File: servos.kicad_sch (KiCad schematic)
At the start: 40 parts, among them J10 Conn_01x03, J11 Conn_01x03, J6 Conn_01x03, J7 Conn_01x03, J8 Conn_01x03, J9 Conn_01x03, U10 INA745A, U11 INA745A, U12 INA745A, U13 INA745A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

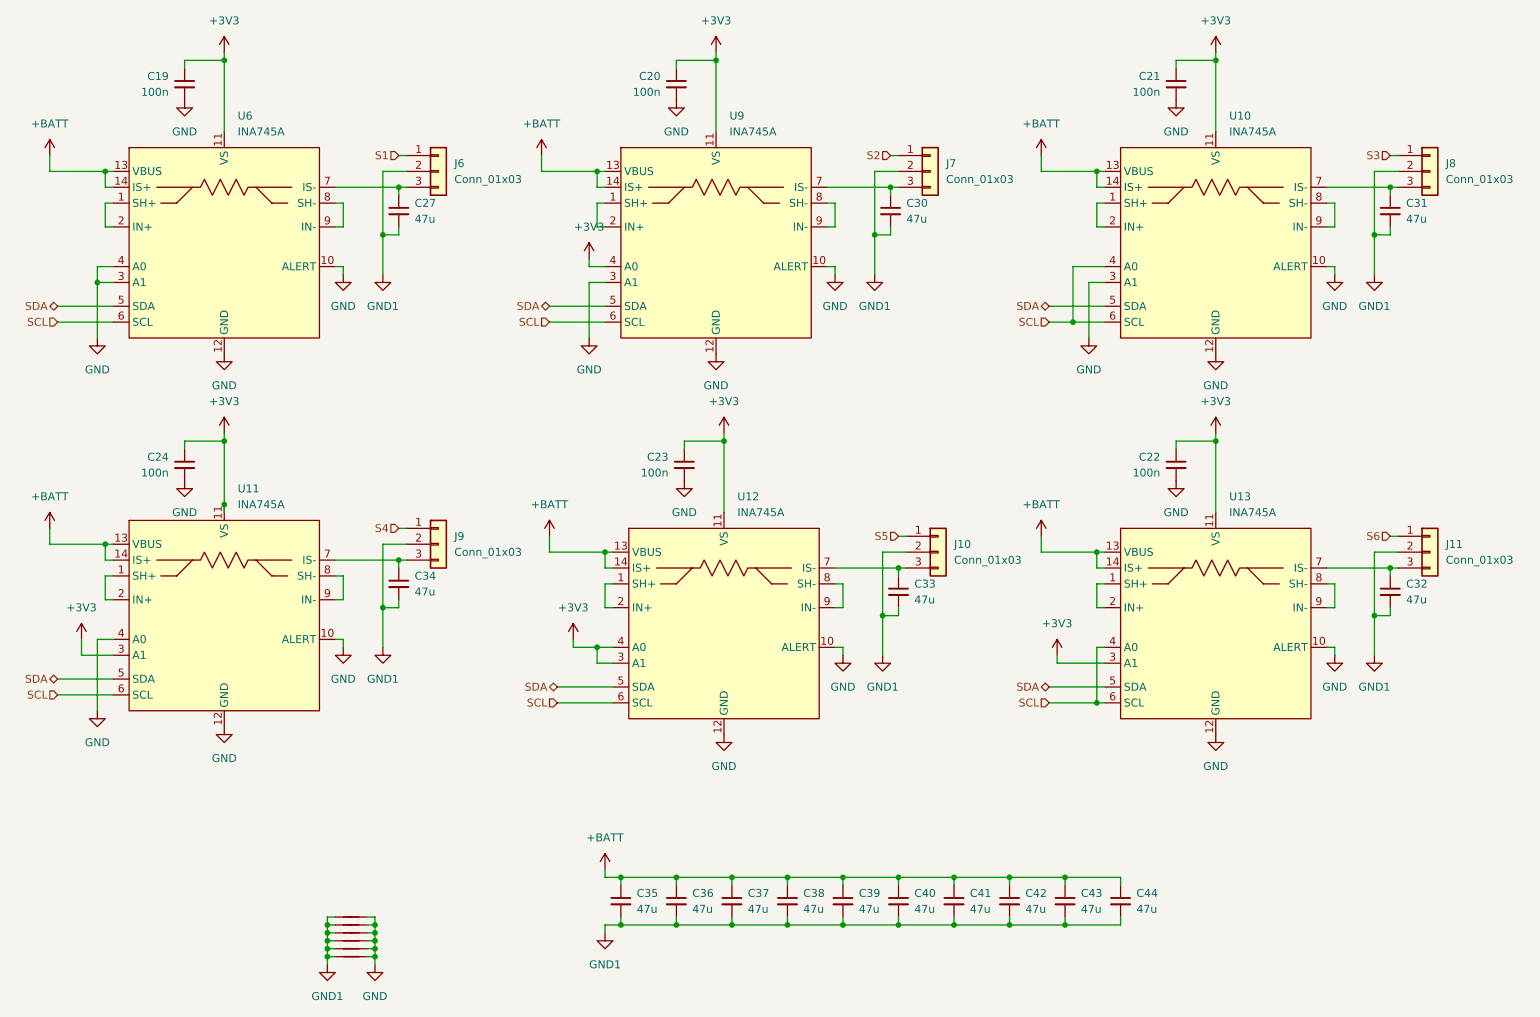
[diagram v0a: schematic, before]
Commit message: switched to global labels for SPI and I2C, added labels for servos
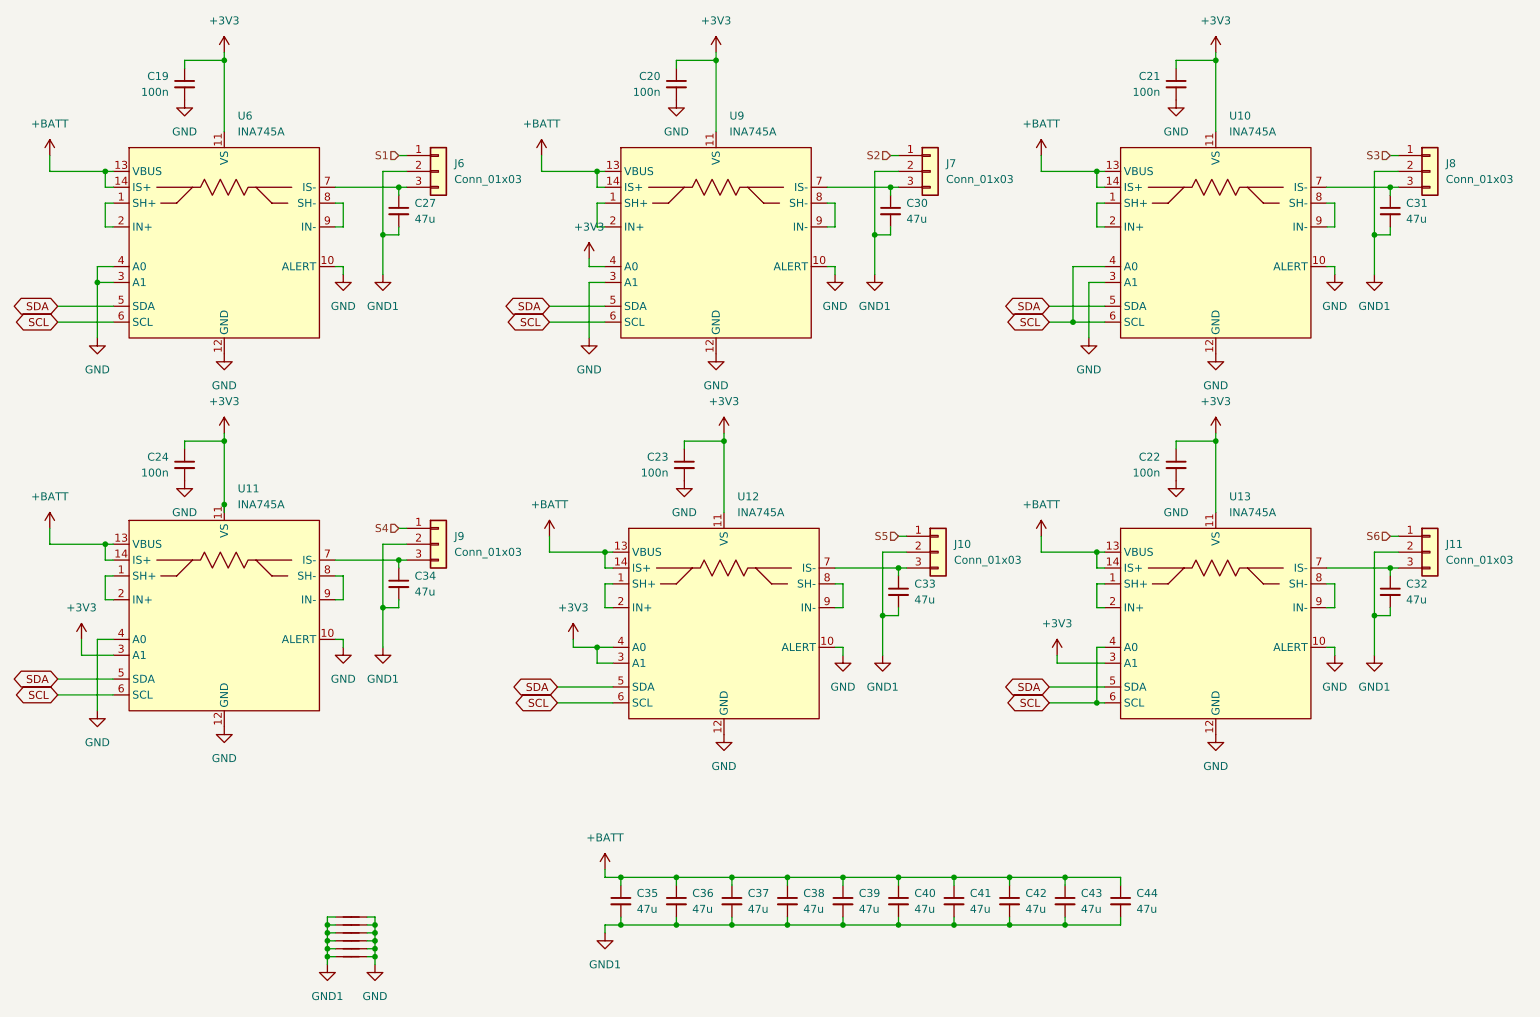
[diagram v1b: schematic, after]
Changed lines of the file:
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@@
 		)
 	)
-	(hierarchical_label "SCL"
-		(shape input)
+	(global_label "SDA"
+		(shape bidirectional)
+		(at 113.03 139.7 180)
+		(fields_autoplaced yes)
+		(effects
+			(font
+				(size 1.27 1.27)
+			)
+			(justify right)
+		)
+		(property "Intersheetrefs" "${INTERSHEET_REFS}"
+			(at 105.3654 139.7 0)
+			(effects
+				(font
+					(size 1.27 1.27)
+				)
+				(justify right)
+				(hide yes)
+			)
+		)
+	)
+	(global_label "SCL"
+		(shape bidirectional)
+		(at 113.03 142.24 180)
+		(fields_autoplaced yes)
+		(effects
+			(font
+				(size 1.27 1.27)
+			)
+			(justify right)
+		)
+		(property "Intersheetrefs" "${INTERSHEET_REFS}"
+			(at 105.4259 142.24 0)
+			(effects
+				(font
+					(size 1.27 1.27)
+				)
+				(justify right)
+				(hide yes)
+			)
+		)
+	)
+	(global_label "SCL"
+		(shape bidirectional)
+		(at 33.02 81.28 180)
+		(fields_autoplaced yes)
+		(effects
+			(font
+				(size 1.27 1.27)
+			)
+			(justify right)
+		)
+		(property "Intersheetrefs" "${INTERSHEET_REFS}"
+			(at 25.4159 81.28 0)
+			(effects
+				(font
+					(size 1.27 1.27)
+				)
+				(justify right)
+				(hide yes)
+			)
+		)
+	)
+	(global_label "SDA"
+		(shape bidirectional)
+		(at 111.76 78.74 180)
+		(fields_autoplaced yes)
+		(effects
+			(font
+				(size 1.27 1.27)
+			)
+			(justify right)
+		)
+		(property "Intersheetrefs" "${INTERSHEET_REFS}"
+			(at 104.0954 78.74 0)
+			(effects
+				(font
+					(size 1.27 1.27)
+				)
+				(justify right)
+				(hide yes)
+			)
+		)
+	)
+	(global_label "SCL"
+		(shape bidirectional)
+		(at 33.02 140.97 180)
+		(fields_autoplaced yes)
+		(effects
+			(font
+				(size 1.27 1.27)
+			)
+			(justify right)
+		)
+		(property "Intersheetrefs" "${INTERSHEET_REFS}"
+			(at 25.4159 140.97 0)
+			(effects
+				(font
+					(size 1.27 1.27)
+				)
+				(justify right)
+				(hide yes)
+			)
+		)
+	)
+	(global_label "SDA"
+		(shape bidirectional)
+		(at 191.77 139.7 180)
+		(fields_autoplaced yes)
+		(effects
+			(font
+				(size 1.27 1.27)
+			)
+			(justify right)
+		)
+		(property "Intersheetrefs" "${INTERSHEET_REFS}"
+			(at 184.1054 139.7 0)
+			(effects
+				(font
+					(size 1.27 1.27)
+				)
+				(justify right)
+				(hide yes)
+			)
+		)
+	)
+	(global_label "SCL"
+		(shape bidirectional)
 		(at 191.77 81.28 180)
-		(effects
-			(font
-				(size 1.27 1.27)
-			)
-			(justify right)
-		)
-	)
-	(hierarchical_label "SDA"
+		(fields_autoplaced yes)
+		(effects
+			(font
+				(size 1.27 1.27)
+			)
+			(justify right)
+		)
+		(property "Intersheetrefs" "${INTERSHEET_REFS}"
+			(at 184.1659 81.28 0)
+			(effects
+				(font
+					(size 1.27 1.27)
+				)
+				(justify right)
+				(hide yes)
+			)
+		)
+	)
+	(global_label "SDA"
+		(shape bidirectional)
+		(at 191.77 78.74 180)
+		(fields_autoplaced yes)
+		(effects
+			(font
+				(size 1.27 1.27)
+			)
+			(justify right)
+		)
+		(property "Intersheetrefs" "${INTERSHEET_REFS}"
+			(at 184.1054 78.74 0)
+			(effects
+				(font
+					(size 1.27 1.27)
+				)
+				(justify right)
+				(hide yes)
+			)
+		)
+	)
+	(global_label "SCL"
+		(shape bidirectional)
+		(at 111.76 81.28 180)
+		(fields_autoplaced yes)
+		(effects
+			(font
+				(size 1.27 1.27)
+			)
+			(justify right)
+		)
+		(property "Intersheetrefs" "${INTERSHEET_REFS}"
+			(at 104.1559 81.28 0)
+			(effects
+				(font
+					(size 1.27 1.27)
+				)
+				(justify right)
+				(hide yes)
+			)
+		)
+	)
+	(global_label "SDA"
 		(shape bidirectional)
 		(at 33.02 138.43 180)
-		(effects
-			(font
-				(size 1.27 1.27)
-			)
-			(justify right)
-		)
-	)
-	(hierarchical_label "SDA"
+		(fields_autoplaced yes)
+		(effects
+			(font
+				(size 1.27 1.27)
+			)
+			(justify right)
+		)
+		(property "Intersheetrefs" "${INTERSHEET_REFS}"
+			(at 25.3554 138.43 0)
+			(effects
+				(font
+					(size 1.27 1.27)
+				)
+				(justify right)
+				(hide yes)
+			)
+		)
+	)
+	(global_label "SCL"
+		(shape bidirectional)
+		(at 191.77 142.24 180)
+		(fields_autoplaced yes)
+		(effects
+			(font
+				(size 1.27 1.27)
+			)
+			(justify right)
+		)
+		(property "Intersheetrefs" "${INTERSHEET_REFS}"
+			(at 184.1659 142.24 0)
+			(effects
+				(font
+					(size 1.27 1.27)
+				)
+				(justify right)
+				(hide yes)
+			)
+		)
+	)
+	(global_label "SDA"
 		(shape bidirectional)
 		(at 33.02 78.74 180)
-		(effects
-			(font
-				(size 1.27 1.27)
-			)
-			(justify right)
-		)
-	)
-	(hierarchical_label "SCL"
-		(shape input)
-		(at 191.77 142.24 180)
-		(effects
-			(font
-				(size 1.27 1.27)
-			)
-			(justify right)
-		)
-	)
-	(hierarchical_label "SCL"
-		(shape input)
-		(at 33.02 81.28 180)
-		(effects
-			(font
-				(size 1.27 1.27)
-			)
-			(justify right)
-		)
-	)
-	(hierarchical_label "SDA"
-		(shape bidirectional)
-		(at 111.76 78.74 180)
-		(effects
-			(font
-				(size 1.27 1.27)
-			)
-			(justify right)
+		(fields_autoplaced yes)
+		(effects
+			(font
+				(size 1.27 1.27)
+			)
+			(justify right)
+		)
+		(property "Intersheetrefs" "${INTERSHEET_REFS}"
+			(at 25.3554 78.74 0)
+			(effects
+				(font
+					(size 1.27 1.27)
+				)
+				(justify right)
+				(hide yes)
+			)
 		)
 	)
@@
 		)
 	)
-	(hierarchical_label "SCL"
-		(shape input)
-		(at 33.02 140.97 180)
-		(effects
-			(font
-				(size 1.27 1.27)
-			)
-			(justify right)
-		)
-	)
-	(hierarchical_label "SDA"
-		(shape bidirectional)
-		(at 113.03 139.7 180)
-		(effects
-			(font
-				(size 1.27 1.27)
-			)
-			(justify right)
-		)
-	)
 	(hierarchical_label "S3"
 		(shape input)
@@
 		)
 	)
-	(hierarchical_label "SDA"
-		(shape bidirectional)
-		(at 191.77 78.74 180)
-		(effects
-			(font
-				(size 1.27 1.27)
-			)
-			(justify right)
-		)
-	)
 	(hierarchical_label "S2"
 		(shape input)
@@
 		(effects
 			(font
-				(size 1.27 1.27)
-			)
-			(justify right)
-		)
-	)
-	(hierarchical_label "SCL"
-		(shape input)
-		(at 111.76 81.28 180)
-		(effects
-			(font
-				(size 1.27 1.27)
-			)
-			(justify right)
-		)
-	)
-	(hierarchical_label "SCL"
-		(shape input)
-		(at 113.03 142.24 180)
-		(effects
-			(font
-				(size 1.27 1.27)
-			)
-			(justify right)
-		)
-	)
-	(hierarchical_label "SDA"
-		(shape bidirectional)
-		(at 191.77 139.7 180)
-		(effects
-			(font

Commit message: switching to electrolytic caps
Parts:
- removed C27, C30, C31, C32, C33, C34, C35, C36, C37, C38, C39, C40, C41, C42, C43, C44: 47u, Capacitor_SMD:C_1206_3216Metric, symbol Device:C_Small
- added C27, C30: 220u, Capacitor_THT:CP_Radial_D5.0mm_P2.00mm, symbol Device:C_Polarized_Small
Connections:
- net +BATT: now also C27.1, C30.1
- net GND1: now also C27.2, C30.2

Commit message: final tweaks
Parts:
- added C31: 220u, Capacitor_THT:CP_Radial_D5.0mm_P2.00mm, symbol Device:C_Polarized_Small
- added D12, D13, D14, D15, D16, D17: D_Zener, Diode_SMD:Nexperia_CFP3_SOD-123W, symbol Device:D_Zener
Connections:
- net +BATT: now also C31.1
- net GND1: now also C31.2, D12.2 (A), D13.2 (A), D14.2 (A), D15.2 (A), D16.2 (A), D17.2 (A)
- net at J9.3 (Pin_3), U11.7 (IS-): now also D15.1 (K)
- net at J6.3 (Pin_3), U6.7 (IS-): now also D12.1 (K)
- net at J7.3 (Pin_3), U9.7 (IS-): now also D13.1 (K)
- net at J11.3 (Pin_3), U13.7 (IS-): now also D17.1 (K)
- net at J10.3 (Pin_3), U12.7 (IS-): now also D16.1 (K)
- net at J8.3 (Pin_3), U10.7 (IS-): now also D14.1 (K)

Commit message: blunkinator
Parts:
- C27, C30, C31: digikey (none) -> 399-ESK227M010AC3AA-ND
- D12, D13, D14, D15, D16, D17: digikey (none) -> 1727-5361-1-ND
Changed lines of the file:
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@@
 			)
 		)
+		(property "digikey" "1727-5361-1-ND"
+			(at 167.64 125.73 90)
+			(effects
+				(font
+					(size 1.27 1.27)
+				)
+				(hide yes)
+			)
+		)
 		(pin "2"
 		)
@@
 			)
 		)
+		(property "digikey" "1727-5361-1-ND"
+			(at 87.63 124.46 90)
+			(effects
+				(font
+					(size 1.27 1.27)
+				)
+				(hide yes)
+			)
+		)
 		(pin "2"
 		)
@@
 			)
 		)
+		(property "digikey" "399-ESK227M010AC3AA-ND"
+			(at 130.81 173.99 0)
+			(effects
+				(font
+					(size 1.27 1.27)
+				)
+				(hide yes)
+			)
+		)
 		(pin "2"
 		)
@@
 			)
 		)
+		(property "digikey" "1727-5361-1-ND"
+			(at 87.63 64.77 90)
+			(effects
+				(font
+					(size 1.27 1.27)
+				)
+				(hide yes)
+			)
+		)
 		(pin "2"
 		)
@@
 			)
 		)
+		(property "digikey" "399-ESK227M010AC3AA-ND"
+			(at 140.97 173.99 0)
+			(effects
+				(font
+					(size 1.27 1.27)
+				)
+				(hide yes)
+			)
+		)
 		(pin "2"
 		)
@@
 			)
 		)
+		(property "digikey" "399-ESK227M010AC3AA-ND"
+			(at 120.65 173.99 0)
+			(effects
+				(font
+					(size 1.27 1.27)
+				)
+				(hide yes)
+			)
+		)
 		(pin "2"
 		)
@@
 			)
 		)
+		(property "digikey" "1727-5361-1-ND"
+			(at 246.38 125.73 90)
+			(effects
+				(font
+					(size 1.27 1.27)
+				)
+				(hide yes)
+			)
+		)
 		(pin "2"
 		)
@@
 			)
 		)
+		(property "digikey" "1727-5361-1-ND"
+			(at 246.38 64.77 90)
+			(effects
+				(font
+					(size 1.27 1.27)
+				)
+				(hide yes)
+			)
+		)
 		(pin "2"
 		)
@@
 			(effects
 				(font
+					(size 1.27 1.27)
+				)
+				(hide yes)
+			)
+		)
+		(property "digikey" "1727-5361-1-ND"
+			(at 166.37 64.77 90)
+			(effects
+				(font
